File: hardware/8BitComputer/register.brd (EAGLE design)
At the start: 100 x 75 mm, 51 parts, among them IC1 SN74LS173ANG4, IC2 SN74LS173ANG4, IC3 SN74LS245NE4, IC4 SN74LS173ANG4, IC5 SN74LS173ANG4, IC6 SN74LS245NE4, J1 BUS OUT, J2 pwr, J4 BUS OUT

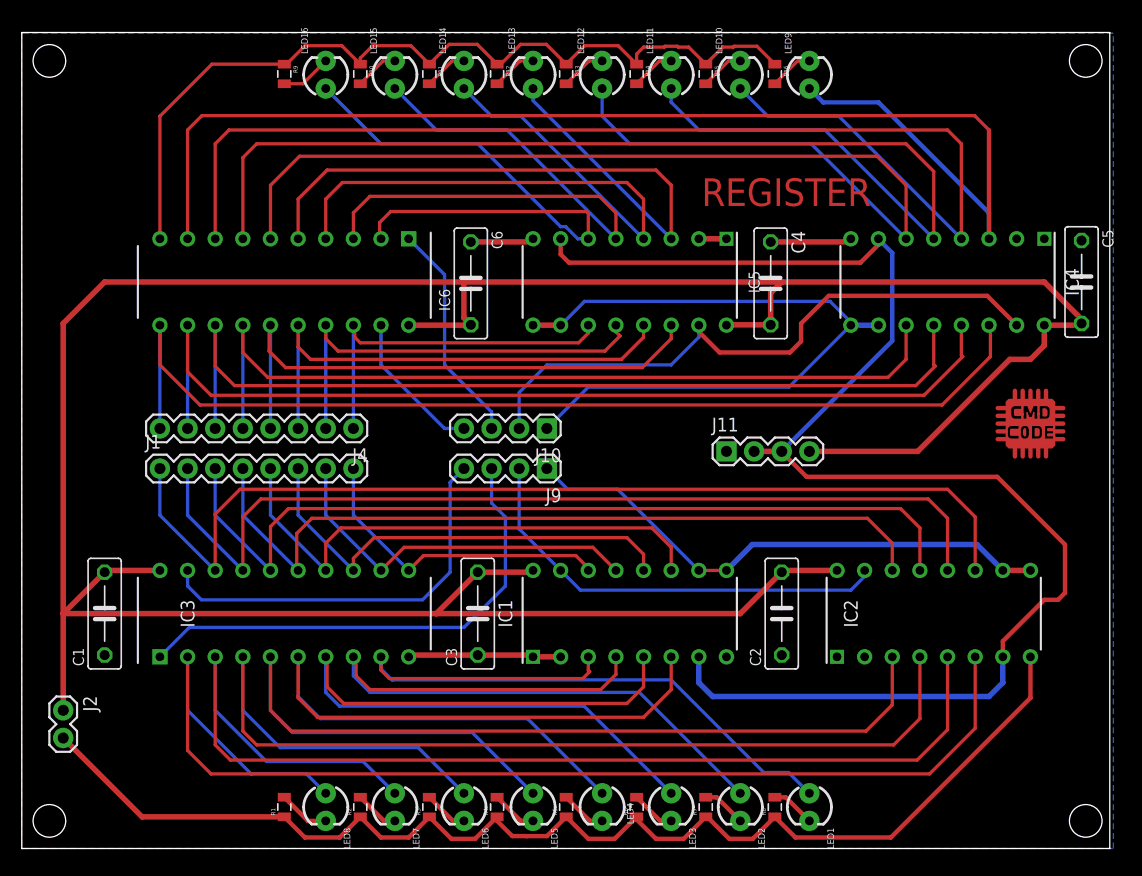
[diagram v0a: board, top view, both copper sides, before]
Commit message: adding static ram chip updated all other boards to remove led resistors that aren't needed
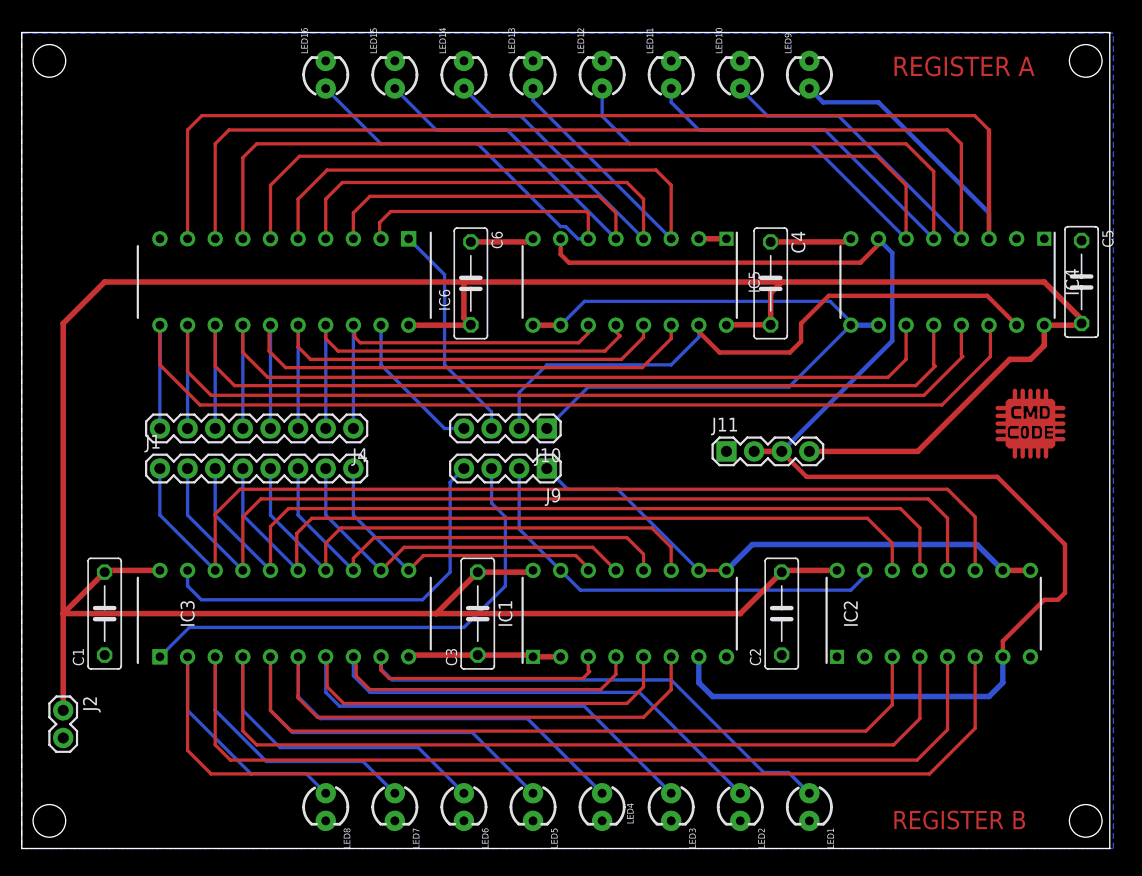
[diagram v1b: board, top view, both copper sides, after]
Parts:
- removed R1, R10, R11, R12, R13, R14, R15, R16, R2, R3, R4, R5, R6, R7, R8, R9: 100 R, passives:0805
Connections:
- removed net N$1: LED9.K, R16.2
- removed net N$2: LED10.K, R15.2
- removed net N$27: LED1.K, R8.2
- removed net N$28: LED2.K, R7.2
- removed net N$29: LED3.K, R6.2
- removed net N$3: LED11.K, R14.2
- removed net N$30: LED4.K, R5.2
- removed net N$31: LED5.K, R4.2
- removed net N$32: LED6.K, R3.2
- removed net N$33: LED7.K, R2.2
- removed net N$34: LED8.K, R1.2
- removed net N$4: LED12.K, R13.2
- removed net N$5: LED13.K, R12.2
- removed net N$6: LED14.K, R11.2
- removed net N$7: LED15.K, R10.2
- removed net N$8: LED16.K, R9.2
- net GND: now also LED1.K, LED10.K, LED11.K, LED12.K, LED13.K, LED14.K, LED15.K, LED16.K, LED2.K, LED3.K, LED4.K, LED5.K, LED6.K, LED7.K, LED8.K, LED9.K; no longer R1.1, R10.1, R11.1, R12.1, R13.1, R14.1, R15.1, R16.1, R2.1, R3.1, R4.1, R5.1, R6.1, R7.1, R8.1, R9.1
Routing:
- net GND: track 224.0 -> 30.0 mm
- net N$34: track 4.71 -> 0.00 mm
- net N$8: track 4.68 -> 0.00 mm
- net N$30: track 4.20 -> 0.00 mm
- net N$31: track 4.20 -> 0.00 mm
- net N$4: track 4.17 -> 0.00 mm
- net N$5: track 4.17 -> 0.00 mm
- net N$33: track 4.07 -> 0.00 mm
- net N$28: track 4.07 -> 0.00 mm
- net N$32: track 4.07 -> 0.00 mm
- net N$29: track 4.07 -> 0.00 mm
- net N$27: track 4.07 -> 0.00 mm
- net N$2: track 4.04 -> 0.00 mm
- net N$7: track 4.04 -> 0.00 mm
- net N$6: track 4.04 -> 0.00 mm
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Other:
- board text added: "REGISTER A"
- board text added: "REGISTER B"
- board text removed: "REGISTER"
